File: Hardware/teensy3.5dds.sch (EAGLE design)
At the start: 96 parts, among them IC1 AD8034, IC10 AD8034, IC11 AD8034, IC12 AD8034, IC2 AD8034, IC8 AD8034, IC9 AD8034, J1 1776275-2, J2 1776275-2, Q1 CSM-7X-DU, X1 1-227161-0

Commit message: hardware: better relay switching circuit
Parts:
- removed R18, R19: (no value), rcl:R-EU_R0805
- added D2, D3: (no value), diode:DIODE-SOD323-W
- added R12, R13: (no value), rcl:R-EU_M0805
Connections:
- removed net N$15: C32.1, R10.2
- removed net N$33: C7.2, C8.-, LED_ON.C, RESET.P$1
- removed net N$34: Q3.C, R19.1
- removed net N$36: Q2.C, R18.1
- removed net N$39: Q2.E, U$3.SW+
- removed net N$40: Q3.E, U$4.SW+
- new net N$12: D2.A, Q3.C, U$4.SW-
- new net N$2: D3.A, Q2.C, U$3.SW-
- net +5V: no longer R18.2, R19.2
- net DAC0_SEL: now also R13.1, R13.2
- net GND: now also C32.1, C7.2, C8.-, LED_ON.C, Q2.E, Q3.E, RESET.P$1; no longer U$3.SW-, U$4.SW-
- net N$10: now also U$3.SIG-, U$4.SIG-
- net N$14: now also R10.2
- net SQUARE_SEL: now also R12.1, R12.2
- net V+: now also D2.C, D3.C, U$3.SW+, U$4.SW+
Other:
- moved on the sheet: C32, D1, IC1A, IC1B, IC2A, IC2B, Q2, Q3, R1, R10, R11, R2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

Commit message: hardware: switch to AD737 instead of peak detector circuit Peak detector needed external impedance decoupling and would not have worked when the offset was different from 0 or when the amplification lead the OpAmps into saturation AD737 is a True-RMS-to-DC converter, which works perfectly for this situation, coming at just 1$ more than an AD8034 IC
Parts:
- removed C32: (no value), rcl:C-EUC0805
- removed D1: (no value), diode:DIODE-SOD323-W
- added IC3: AD8034, linear:TL082D
- added IC4: AD737KRZ-R7, AD737KRZ-R7:AD737KRZ-R7
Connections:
- net AMPL_MEASURE: now also IC3B.OUT; no longer IC2B.OUT
- net GND: now also IC4.COM, IC4.POWER_DOWN; no longer C32.1
- net N$14: now also IC4.OUTPUT, R10.1; no longer C32.2, D1.C, R10.2
- net N$16: now also IC3B.-IN, R10.2; no longer IC2B.-IN, R10.1
- net N$22: now also IC3B.+IN; no longer IC2B.+IN
- net N$9: now also IC4.VIN; no longer D1.A
- net V+: now also IC4.+VS
- net V-: now also IC4.-VS, IC4.CAV
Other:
- note added: "DECOUPLING/FILTER CAPACITORS"
- note added: "PLACE ONE CLOSE TO EACH OPAMP AND AD737 IC SUPPLY"
- note added: "PULL_UP RESISTOR ON INTERRUPT IS ENABLED IN SOFTWARE (PINMODE INPUT_PULLUP)"
- note added: "R4 AND R5 CALIBRATED TO OUTPUT 2.5V R6 AND R7 CALIBRATED TO OFFER A 1/5 RATIO"
- note removed: "DECOUPLING CAPS"
- note removed: "PLACE ONE CLOSE TO EACH OPAMP IC SUPPLY"
- note removed: "R4 AND R5 CALIBRATED TO OUTPUT 2.5V R6 AND R7CALIBRATED TO OFFER A 1/5 RATIO"
- moved on the sheet: IC1B, R10, R11, R8, R9, X1

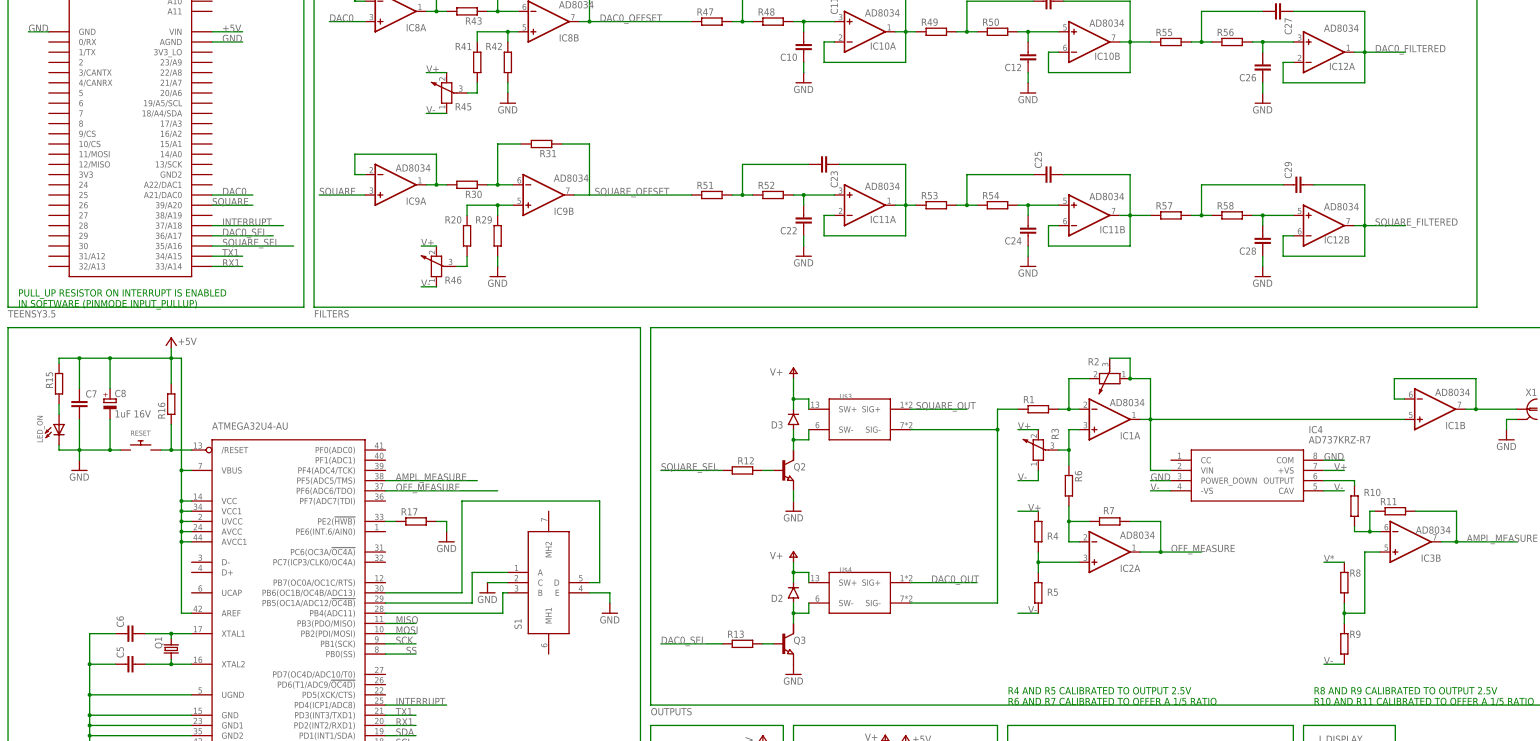
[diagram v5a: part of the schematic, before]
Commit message: hardware: change some trimmers and potentiometers
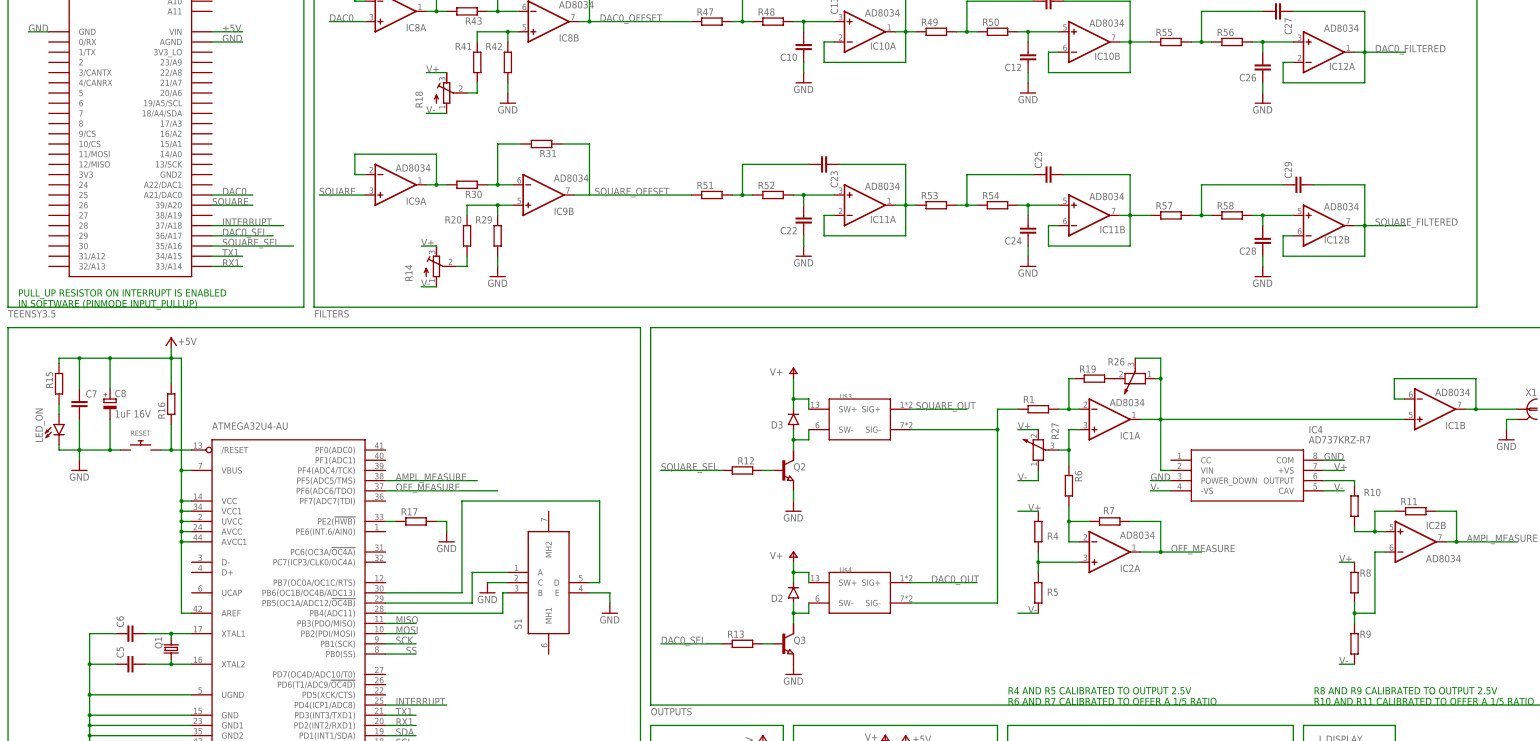
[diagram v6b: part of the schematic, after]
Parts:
- removed IC3: AD8034, linear:TL082D
- removed R2, R3, R45, R46: (no value), rcl:POTENTIOMETER_PT-10
- added R14, R18: (no value), rcl:R-TRIMM3296W
- added R19: (no value), rcl:R-EU_R0805
- added R26, R27: POTENTIOMETER_VERTICAL, Potentiometer_vertical:POTENTIOMETER_VERTICAL
- LED_ON: device adafruit:LEDCHIP-LED0603 -> led:LEDCHIPLED_1206
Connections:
- removed net V*: R8.1
- new net N$15: R19.2, R26.2
- net AMPL_MEASURE: now also IC2B.OUT; no longer IC3B.OUT
- net N$16: now also IC2B.+IN; no longer IC3B.-IN
- net N$22: now also IC2B.-IN; no longer IC3B.+IN
- net N$3: now also R27.3; no longer R3.3
- net N$5: now also R19.1; no longer R2.2
- net N$56: now also R18.S; no longer R45.3
- net N$60: now also R14.S; no longer R46.3
- net N$9: now also R26.1, R26.3; no longer R2.1, R2.3
- net V+: now also R14.E, R18.E, R27.2, R8.1; no longer R3.2, R45.2, R46.2
- net V-: now also R14.A, R18.A, R27.1; no longer R3.1, R45.1, R46.1
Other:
- moved on the sheet: R11, R8, R9

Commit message: hardware: board v0.1
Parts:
- removed R26: POTENTIOMETER_VERTICAL, Potentiometer_vertical:POTENTIOMETER_VERTICAL
- added U$6: POTENTIOMETER_VERTICAL, Potentiometer_vertical:POTENTIOMETER_VERTICAL
- renumbered R27 to U$5
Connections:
- removed net N$6: IC1B.-IN, IC1B.OUT, X1.1
- new net N$17: Q2.B, R12.2
- new net N$18: Q3.B, R13.2
- new net N$19: IC1A.-IN, IC1A.OUT, X1.1
- net DAC0_SEL: no longer Q3.B, R13.2
- net GND: no longer U$2.GND, U$2.GND2, U$2.GND3, U$2.UGND
- net N$15: now also U$6.1; no longer R26.2
- net N$16: now also IC2B.-IN; no longer IC2B.+IN
- net N$22: now also IC2B.+IN; no longer IC2B.-IN
- net N$3: now also IC1B.+IN; no longer IC1A.+IN
- net N$5: now also IC1B.-IN; no longer IC1A.-IN
- net N$67: now also R57.1; no longer R53.1
- net N$70: now also R51.1; no longer R57.1
- net N$9: now also IC1A.+IN, IC1B.OUT, U$6.2, U$6.3; no longer IC1A.OUT, IC1B.+IN, R26.1, R26.3
- net RX1: now also U$1.32/A13; no longer U$1.33/A14
- net SQUARE_OFFSET: now also R53.1; no longer R51.1
- net SQUARE_SEL: no longer Q2.B, R12.2
- net TX1: now also U$1.31/A12; no longer U$1.34/A15
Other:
- moved on the sheet: C22, C23, C24, C25, IC11A, IC11B, IC1A, IC1B, IC2B, R19, R51, R52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

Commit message: hardware: board v0.3 could it by shrinked a little bit on the shorter side?
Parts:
- added C32, C35: 100n, rcl:C-EUC0805
- added C34: 100n, rcl:C-EUC1206
- C7: value 100n 16V -> 1u; device rcl:C-EUC0805 -> rcl:C-EUC1206
- C8: value 1uF 16V -> 1u; device rcl:CPOL-EU085CS-1AR -> rcl:C-EUC0805
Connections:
- net +5V: now also C32.1, C34.1, C35.1, C8.1; no longer C8.+
- net GND: now also C32.2, C34.2, C35.2, C8.2, U$2.GND, U$2.GND2, U$2.GND3; no longer C8.-
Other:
- moved on the sheet: C1, C13, C14, C15, C16, C17, C18, C19, C2, C20, C3, C30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
